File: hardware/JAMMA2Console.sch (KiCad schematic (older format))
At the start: 35 parts, among them J1 Conn_02x28_JAMMA, J2 DS1038-15FBNSiA74-0CC, J3 SCART-F, J4 DF1BZ-34DP-2.5DSA, J5 AudioJack3, J6 DS1037-15FNAKT74-0CC, J7 DS1037-15FNAKT74-0CC, J8 Phoenix PTS 1,5/4-5.0, J9 USB_B_Mini, U1 USBLC6-2P6, U2 LD1117-3.3

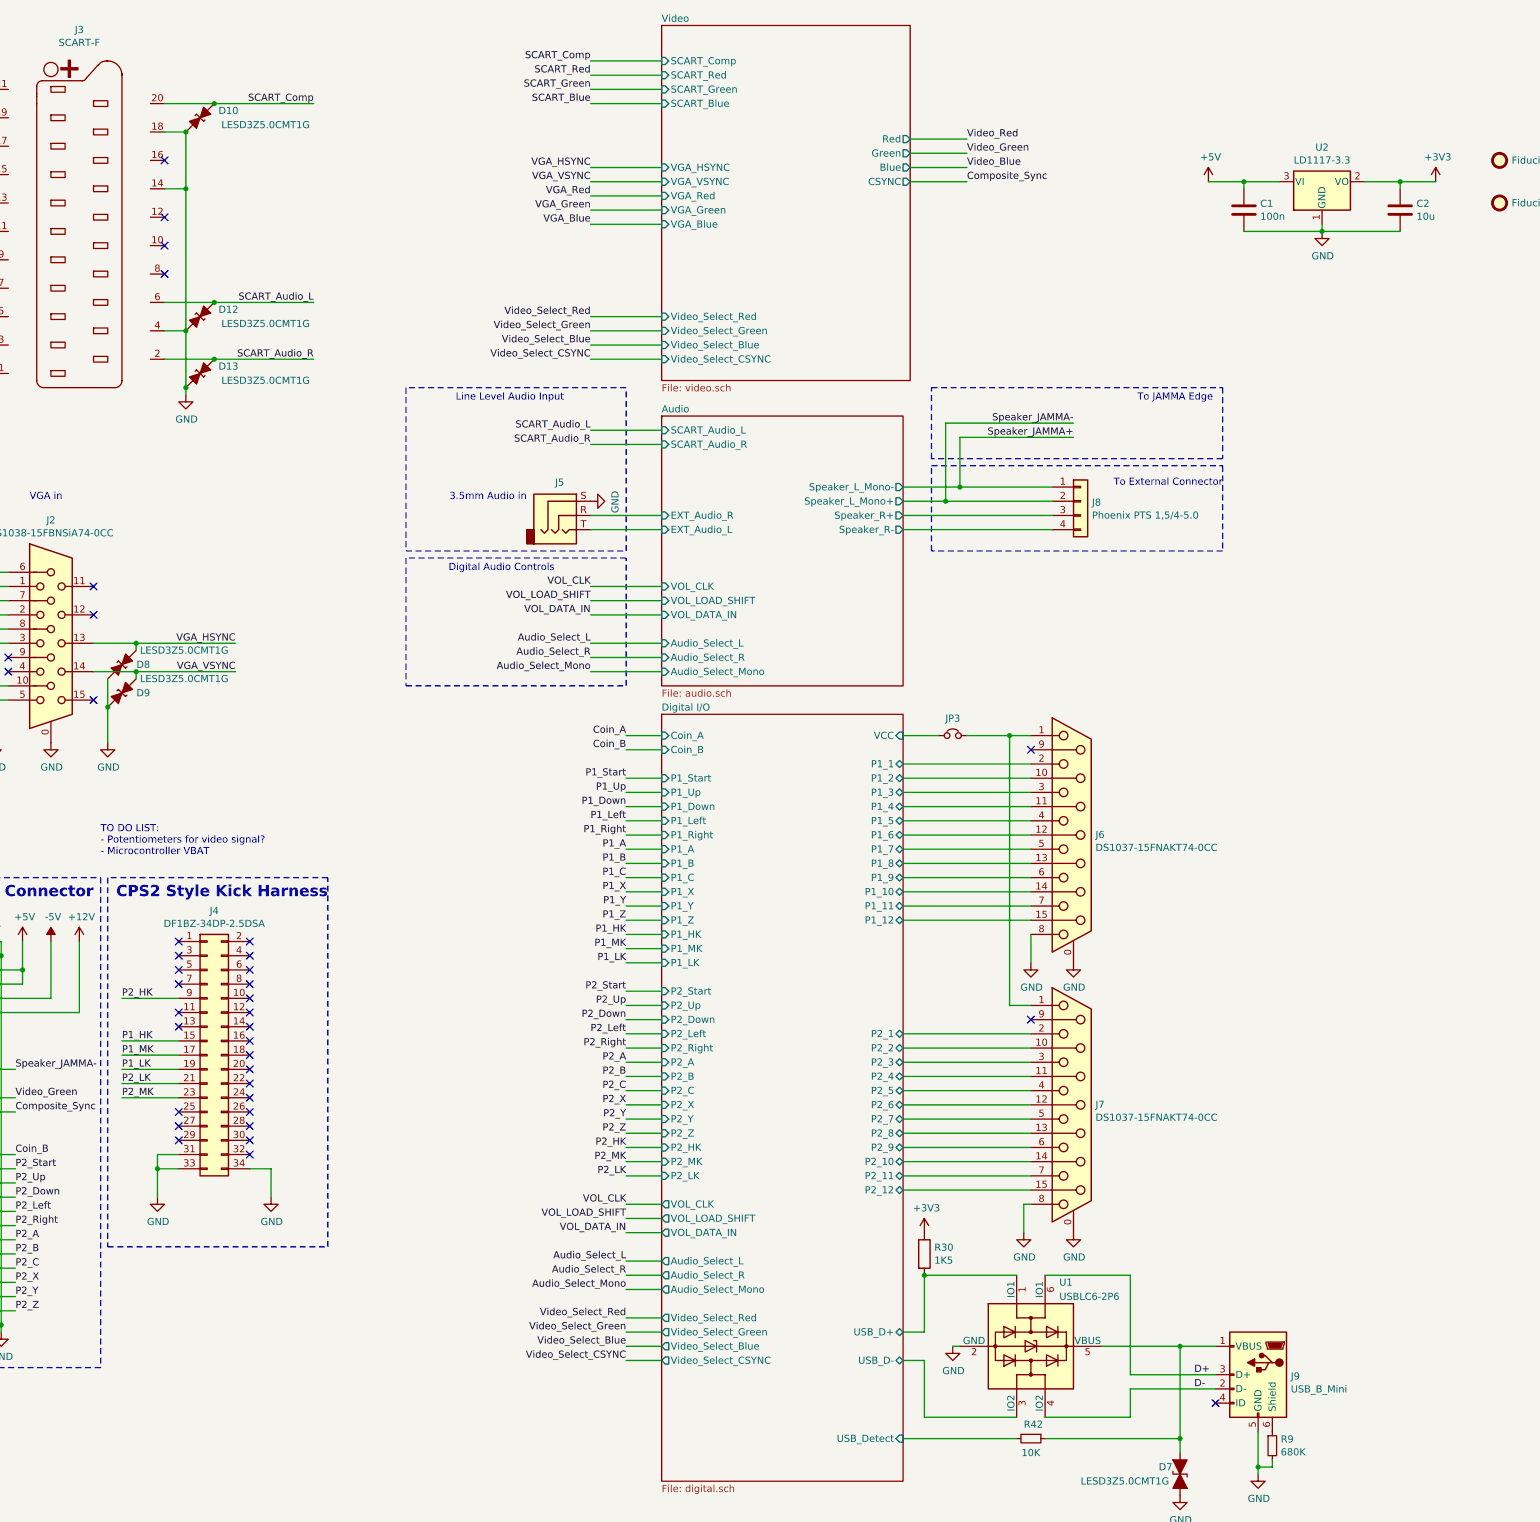
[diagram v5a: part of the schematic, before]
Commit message: Completing layout & minor edits for the main PCB. Added a project for the adapters to plug controllers into.
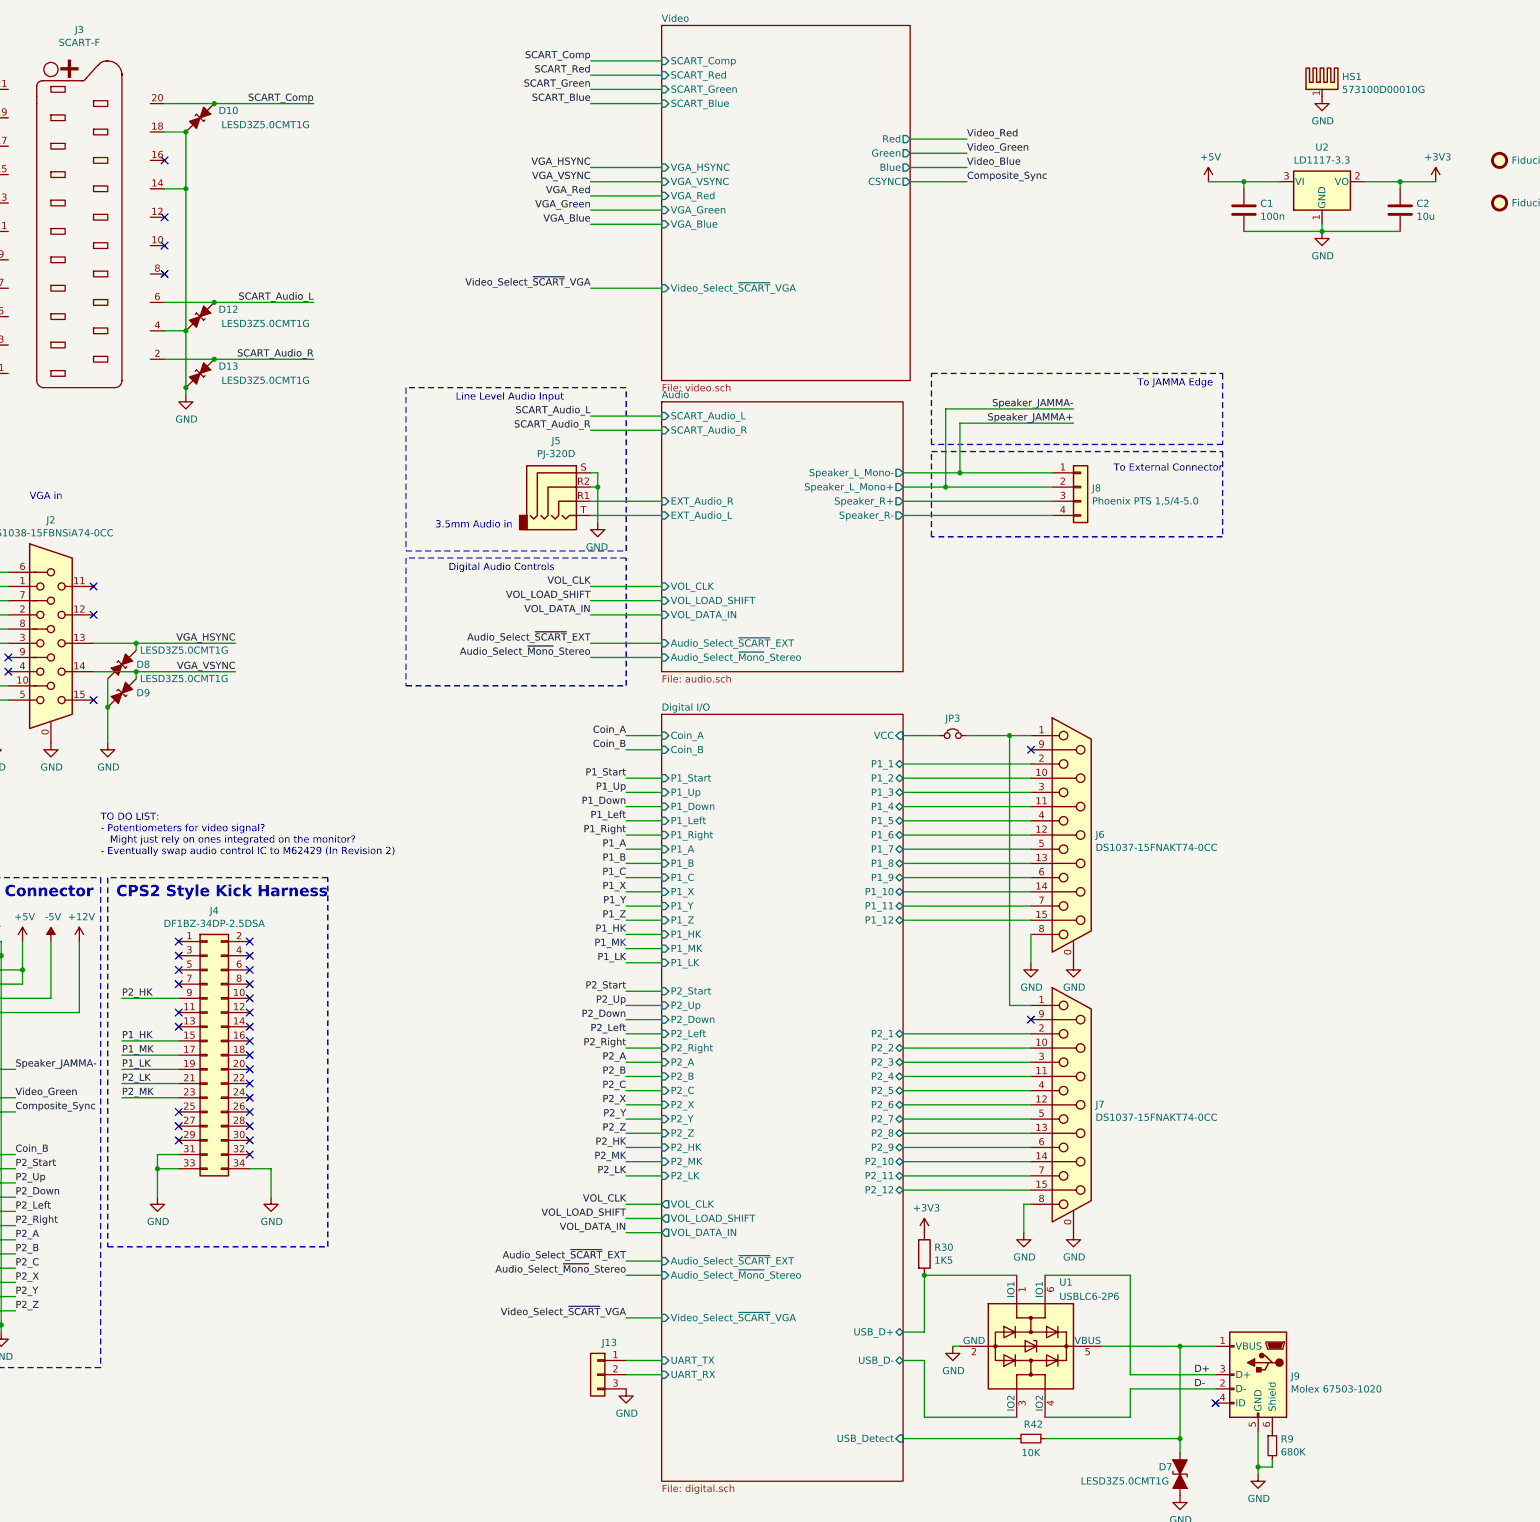
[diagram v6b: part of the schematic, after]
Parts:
- removed J5: AudioJack3, Connector_Audio:Jack_3.5mm_CUI_SJ-3523-SMT_Horizontal, symbol Connector:AudioJack3
- added HS1: 573100D00010G, Console2JAMMA:Heatsink_AAVID_573100D000x0G_TO-252, symbol Mechanical:Heatsink_Pad
- added J13: Conn_01x03, Connector_PinHeader_2.54mm:PinHeader_1x03_P2.54mm_Vertical, symbol Connector_Generic:Conn_01x03
- added J5: PJ-320D, Connector_Audio:Jack_3.5mm_PJ320D_Horizontal, symbol Connector:AudioJack4
- J3: footprint Console2JAMMA:Conn_SCART_Female_Right_Angle -> Console2JAMMA:Conn_SCART_CS-107_Right_Angle_Female
- J4: footprint Connector_PinHeader_2.54mm:PinHeader_2x17_P2.54mm_Vertical -> Console2JAMMA:Conn_02x17_DF1BZ-34DP-2.5DSA
- J9: value USB_B_Mini -> Molex 67503-1020; footprint Connector_USB:USB_Mini-B_Lumberg_2486_01_Horizontal -> Console2JAMMA:USB_Mini-B_Molex_657031020_Horizontal
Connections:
- net Audio/EXT_Audio_L: now also J5.T
- net Audio/EXT_Audio_R: now also J5.R1
- net GND: now also HS1.1, J13.3 (Pin_3), J5.R2, J5.S
- new net Digital I/O/UART_RX: J13.2 (Pin_2)
- new net Digital I/O/UART_TX: J13.1 (Pin_1)
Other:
- note added: "TO DO LIST:\n- Potentiometers for video signal?\n Might just rely on ones integrated on the monitor?\n- Eventually swap audio control IC to M62429 (In Revision 2)"
- note removed: "TO DO LIST:\n- Potentiometers for video signal?\n- Microcontroller VBAT\n"
- moved on the sheet: J8

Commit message: Started major rework on the Audio section (chose the wrong amplifier as it can't drive 4Ohm loads) Moved over to nightly Kicad v 5.9 versions. Was a mistake to do, but will look into reverting another time.
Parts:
- R30: footprint Resistor_SMD:R_0603_1608Metric -> Resistor_SMD:R_0402_1005Metric
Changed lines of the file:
@@
 Sheet 1 4
 Title "JAMMA2Console"
-Date "2020-04-20"
-Rev "1"
+Date "2020-05-01"
+Rev "2"
 Comp "Gold"
 Comment1 ""
@@
 F 0 "R30" H 8570 9296 50  0000 L CNN
 F 1 "1K5" H 8570 9205 50  0000 L CNN
-F 2 "Resistor_SMD:R_0603_1608Metric" V 8430 9250 50  0001 C CNN
+F 2 "Resistor_SMD:R_0402_1005Metric" V 8430 9250 50  0001 C CNN
 F 3 "~" H 8500 9250 50  0001 C CNN
 	1    8500 9250
